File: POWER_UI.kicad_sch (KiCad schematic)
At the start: 46 parts

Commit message: fixed #1 , added protection circuit 5V selector jumper
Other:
- note added: "I2C I/O expander"
- note added: "Insulated high voltage input (max ??)"
- note added: "Insulated output"
- company: (none) -> Filippo Castellan, Alan Masutti
- title: (none) -> Think Embedded dev Board
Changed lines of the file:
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@@
 	(generator_version "9.0")
 	(paper "A4")
+	(title_block
+		(title "Think Embedded dev Board")
+		(date "2026-03-12")
+		(rev "1.0")
+		(company "Filippo Castellan, Alan Masutti")
+	)
 	(rectangle
 		(start 212.09 21.59)
@@
 		(stroke
 			(width 0)
-			(type default)
+			(type dash_dot)
 		)
 		(fill
@@
 		(stroke
 			(width 0)
-			(type default)
+			(type dash_dot)
 		)
 		(fill
@@
 		(stroke
 			(width 0)
-			(type default)
+			(type dash_dot)
 		)
 		(fill
@@
 		(stroke
 			(width 0)
-			(type default)
+			(type dash_dot)
 		)
 		(fill
@@
 		)
 	)
+	(text "Insulated output"
+		(exclude_from_sim no)
+		(at 219.964 20.066 0)
+		(effects
+			(font
+				(size 1.27 1.27)
+			)
+		)
+	)
+	(text "Insulated high voltage input (max ??)"
+		(exclude_from_sim no)
+		(at 132.842 20.066 0)
+		(effects
+			(font
+				(size 1.27 1.27)
+			)
+		)
+	)
+	(text "I2C I/O expander"
+		(exclude_from_sim no)
+		(at 33.782 20.32 0)
+		(effects
+			(font
+				(size 1.27 1.27)
+			)
+		)
+	)

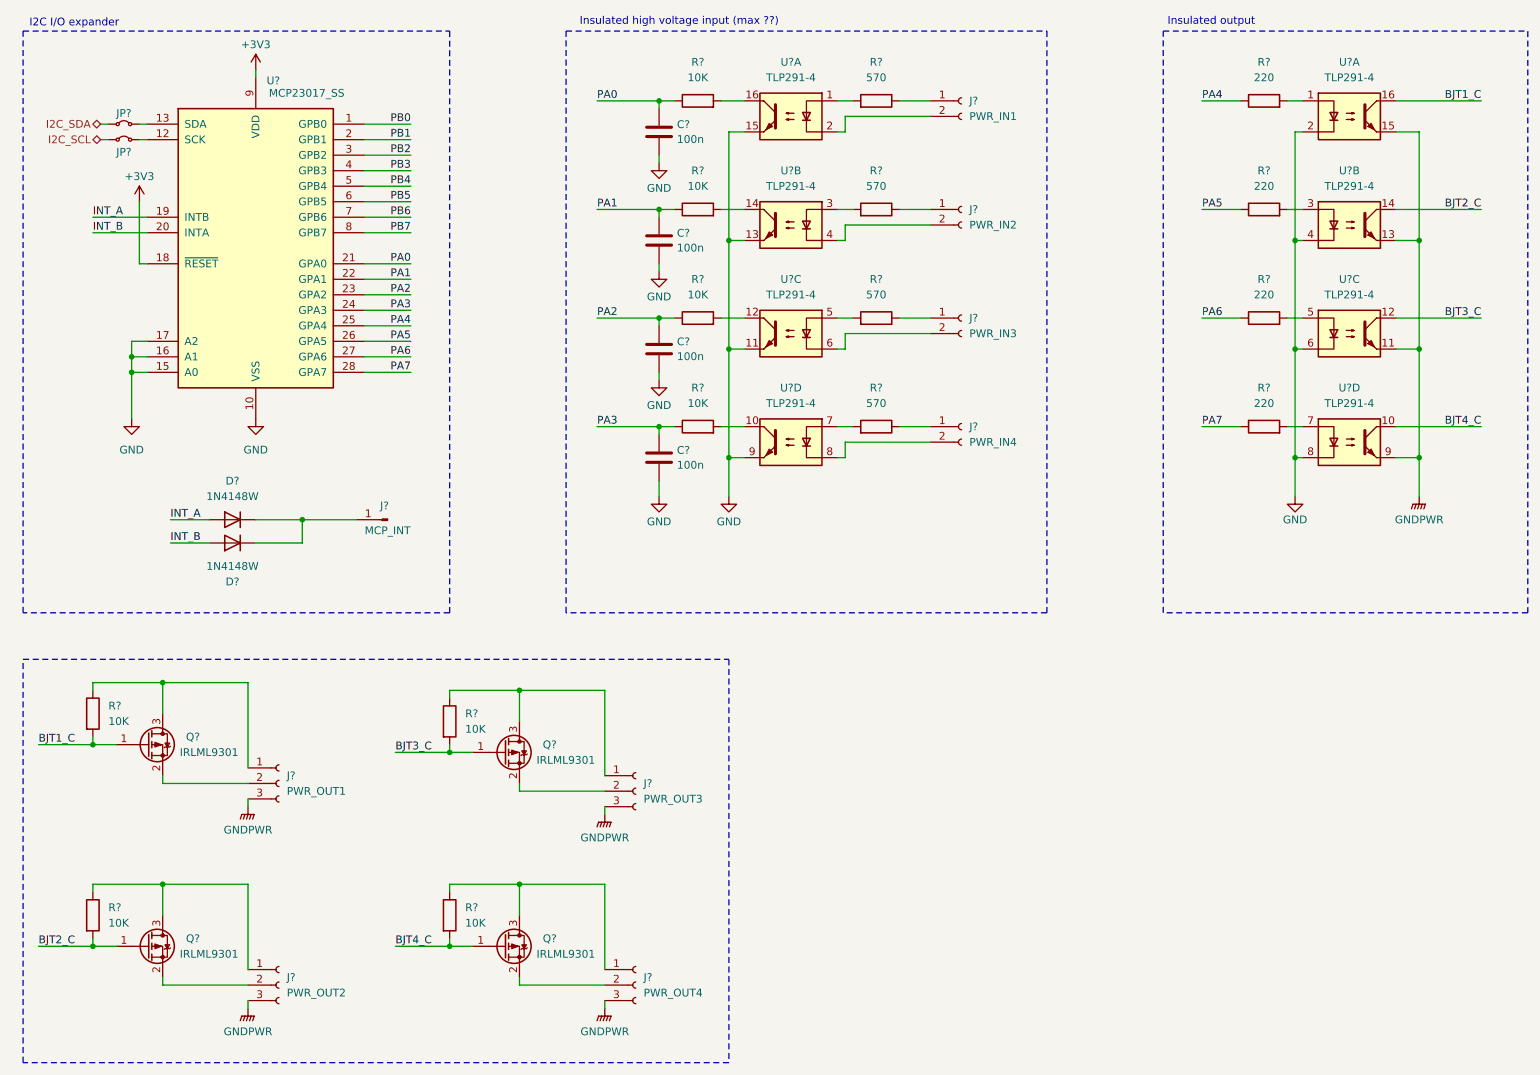
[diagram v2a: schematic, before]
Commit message: Changed the grounding of the opto-coupled power stage + Added UI connectors + Removed a Diode on the Power Sheet (Fixes #3)
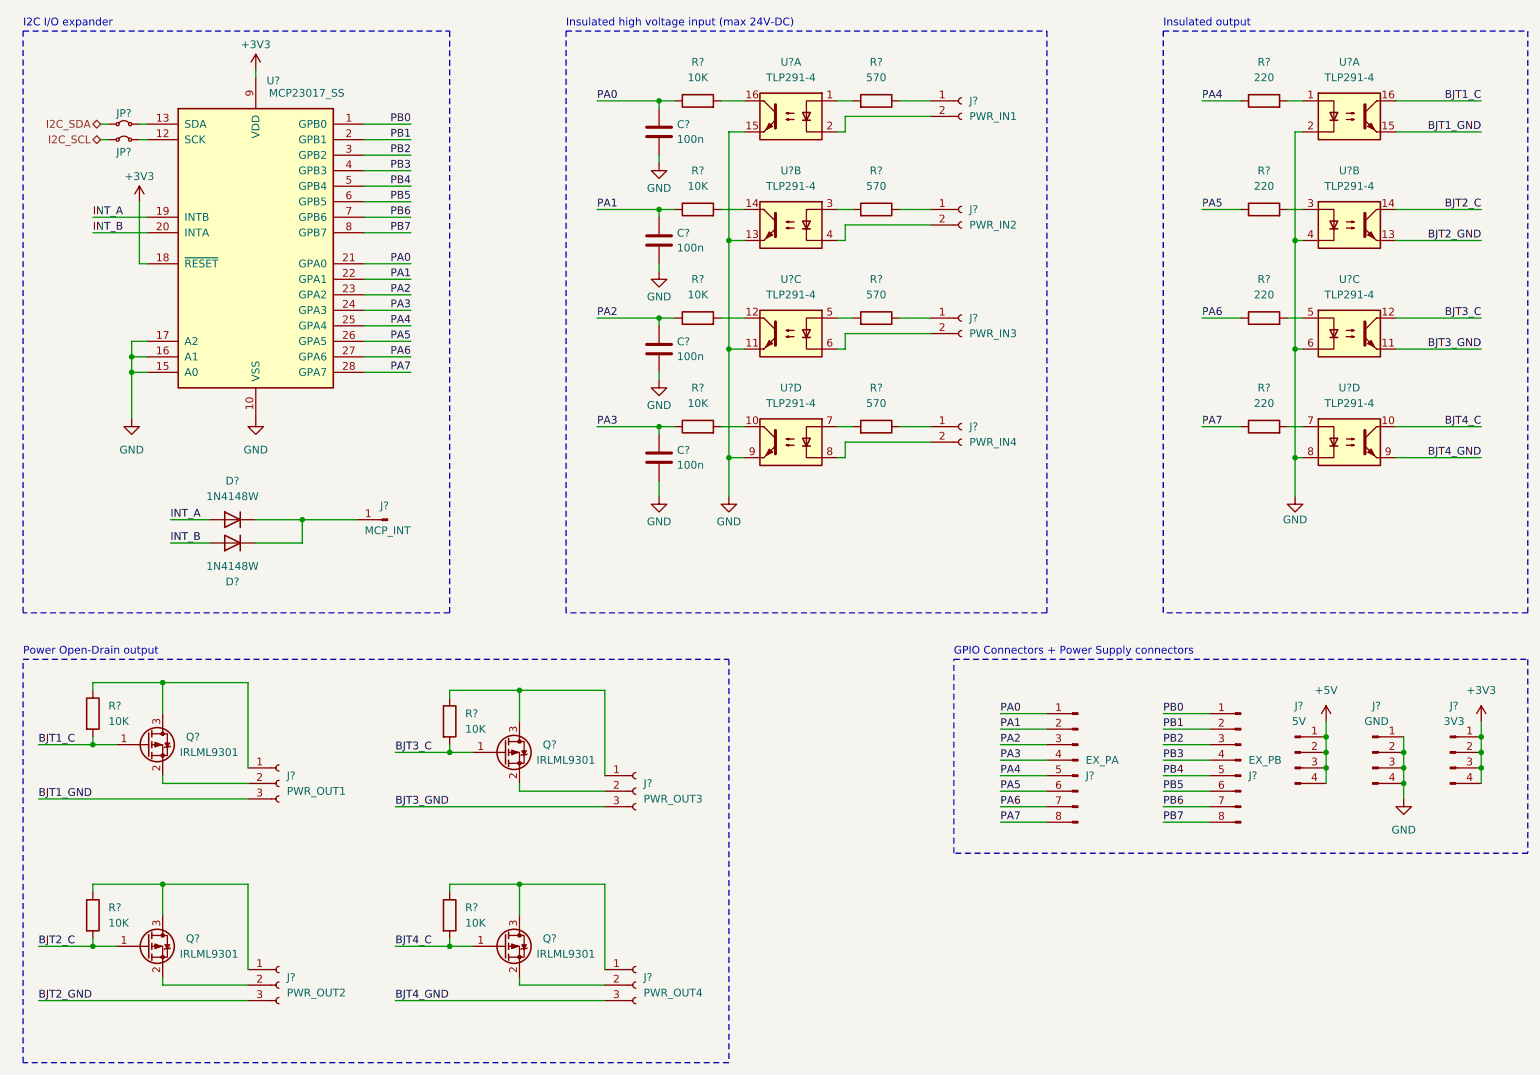
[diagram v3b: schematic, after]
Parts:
- added J?: GND, symbol Connector:Conn_01x04_Pin
- added J?: EX_PA, symbol Connector:Conn_01x08_Pin
- added J?: 3V3, symbol Connector:Conn_01x04_Pin
- added J?: EX_PB, symbol Connector:Conn_01x08_Pin
- added J?: 5V, symbol Connector:Conn_01x04_Pin
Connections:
- net +3V3: now also J?.1 (Pin_1), J?.2 (Pin_2), J?.3 (Pin_3), J?.4 (Pin_4)
- net GND: now also J?.1 (Pin_1), J?.2 (Pin_2), J?.3 (Pin_3), J?.4 (Pin_4)
- net PA0: now also J?.1 (Pin_1)
- net PA1: now also J?.2 (Pin_2)
- net PA2: now also J?.3 (Pin_3)
- net PA3: now also J?.4 (Pin_4)
- net PA4: now also J?.5 (Pin_5)
- net PA5: now also J?.6 (Pin_6)
- net PA6: now also J?.7 (Pin_7)
- net PA7: now also J?.8 (Pin_8)
- net PB0: now also J?.1 (Pin_1)
- net PB1: now also J?.2 (Pin_2)
- net PB2: now also J?.3 (Pin_3)
- net PB3: now also J?.4 (Pin_4)
- net PB4: now also J?.5 (Pin_5)
- net PB5: now also J?.6 (Pin_6)
- net PB6: now also J?.7 (Pin_7)
- net PB7: now also J?.8 (Pin_8)
- removed net GNDPWR: J?.3 (Pin_3), J?.3 (Pin_3), J?.3 (Pin_3), J?.3 (Pin_3), U?.11, U?.13, U?.15, U?.9
- new net +5V: J?.1 (Pin_1), J?.2 (Pin_2), J?.3 (Pin_3), J?.4 (Pin_4)
- new net BJT1_GND: J?.3 (Pin_3), U?.15
- new net BJT2_GND: J?.3 (Pin_3), U?.13
- new net BJT3_GND: J?.3 (Pin_3), U?.11
- new net BJT4_GND: J?.3 (Pin_3), U?.9
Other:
- note added: "GPIO Connectors + Power Supply connectors"
- note added: "Insulated high voltage input (max 24V-DC)"
- note added: "Power Open-Drain output"
- note removed: "Insulated high voltage input (max ??)"

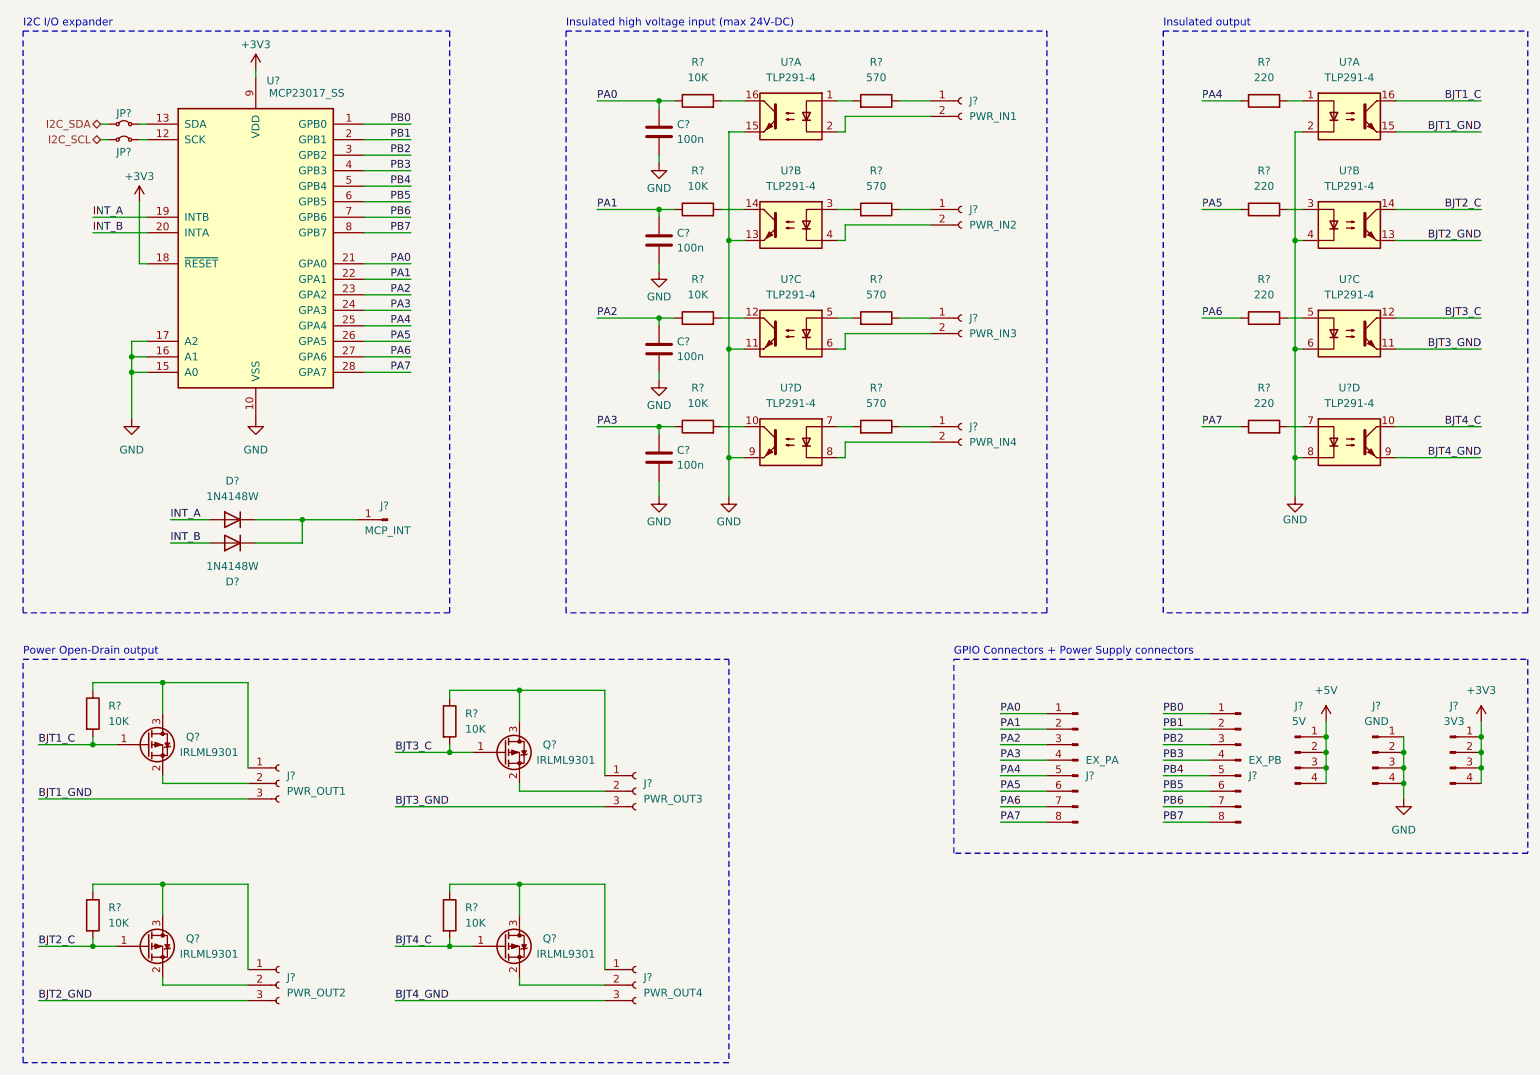
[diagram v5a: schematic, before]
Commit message: Fixed some schematic issues
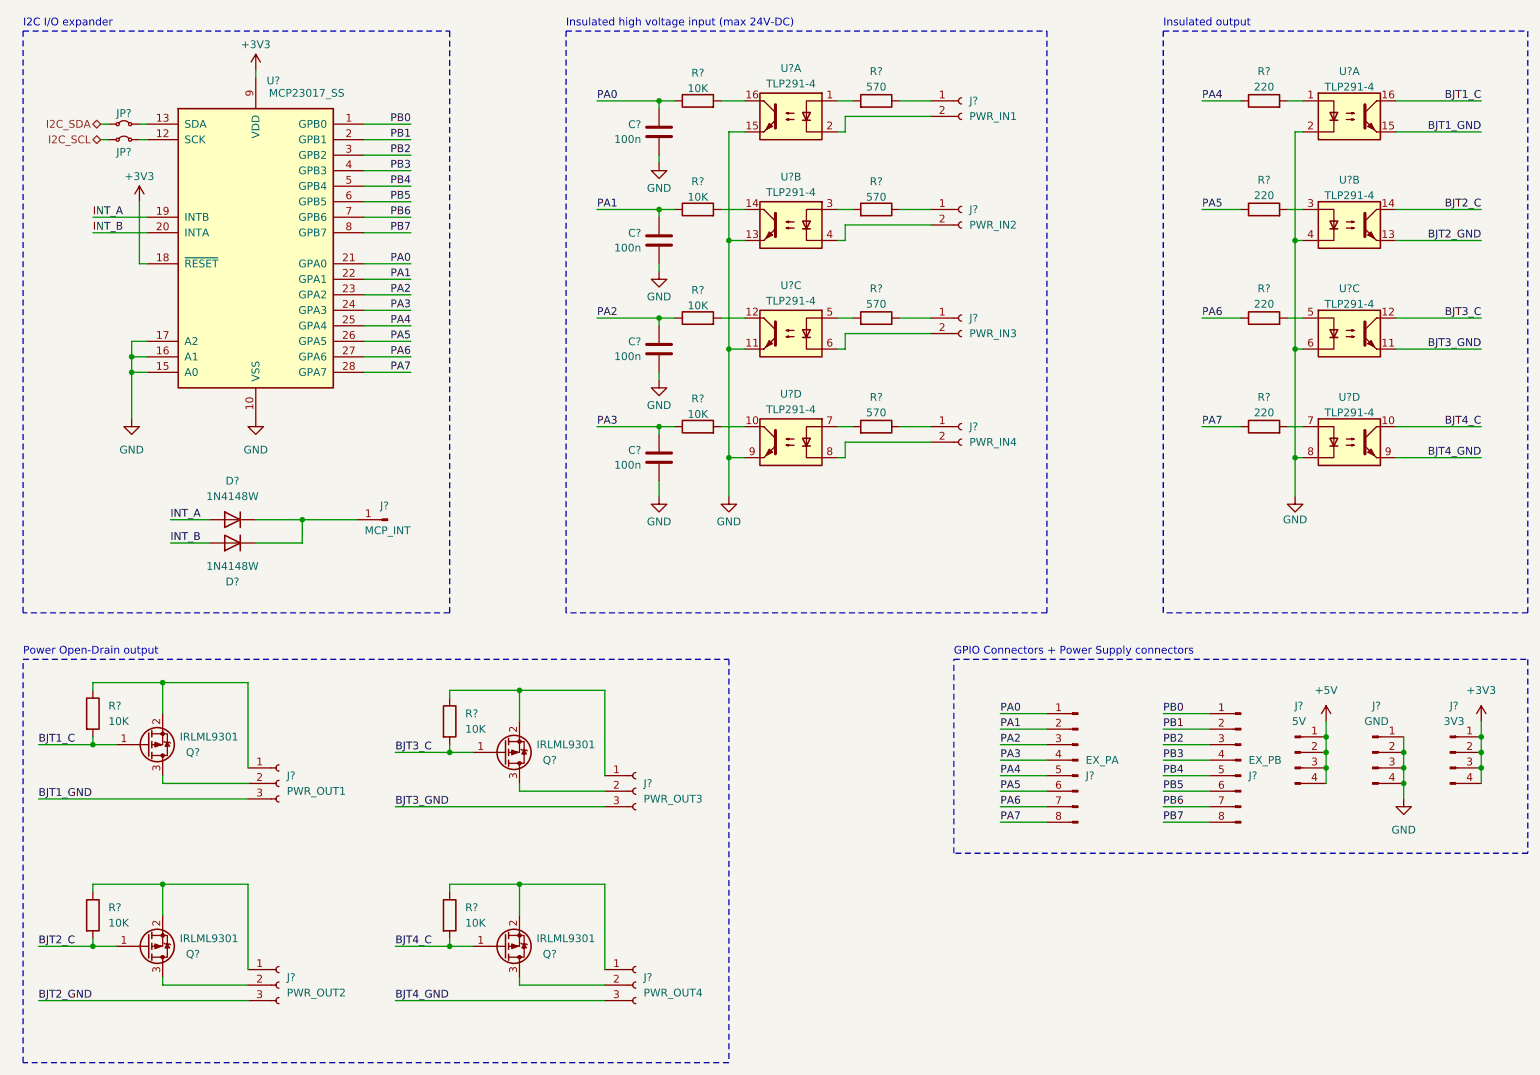
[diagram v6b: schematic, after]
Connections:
- net at J?.1 (Pin_1), R?.1: now also Q?.2 (S); no longer Q?.3 (D) (x2)
- net at J?.2 (Pin_2): now also Q?.3 (D); no longer Q?.2 (S) (x2)
- net at Q?.2 (S): now also J?.1 (Pin_1), R?.1; no longer J?.2 (Pin_2) (x2)
- new net: J?.2 (Pin_2), Q?.3 (D) (x2)

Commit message: Referenced the shematic and started the sourcing part
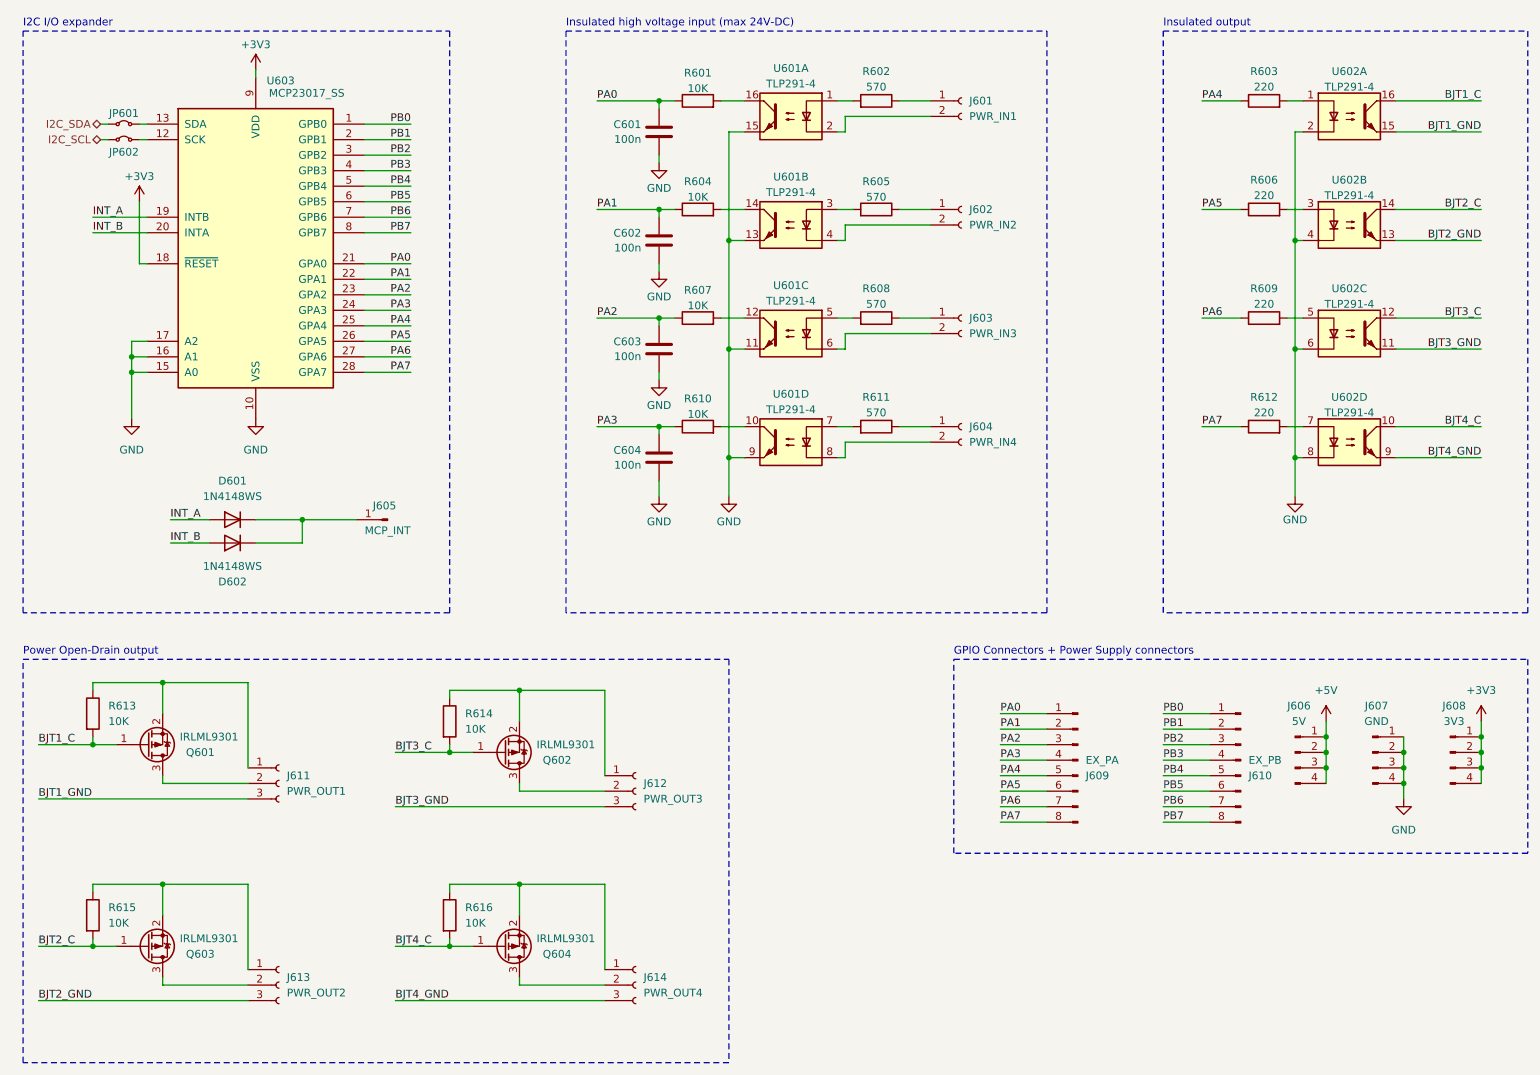
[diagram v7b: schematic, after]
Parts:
- C601, C602, C603, C604: renamed from C?; footprint Capacitor_SMD:C_0805_2012Metric_Pad1.18x1.45mm_HandSolder -> Capacitor_SMD:C_0603_1608Metric_Pad1.08x0.95mm_HandSolder; LCSC (none) -> C14663
- D601, D602: renamed from D?; value 1N4148W -> 1N4148WS; footprint Diode_SMD:D_SOD-123 -> Diode_SMD:D_SOD-323_HandSoldering; LCSC (none) -> C2128
- J601, J602, J603, J604: renamed from J?; footprint (none) -> Connector_PinHeader_2.54mm:PinHeader_1x02_P2.54mm_Vertical; LCSC (none) -> C492401
- J605: renamed from J?; footprint (none) -> Connector_PinHeader_2.54mm:PinHeader_1x01_P2.54mm_Vertical; LCSC (none) -> C492400
- J606, J607, J608: renamed from J?; footprint (none) -> Connector_PinHeader_2.54mm:PinHeader_1x04_P2.54mm_Vertical; LCSC (none) -> C492403
- J609, J610: renamed from J?; footprint (none) -> Connector_PinHeader_2.54mm:PinHeader_1x08_P2.54mm_Vertical; LCSC (none) -> C492407
- J611, J612, J613, J614: renamed from J?; footprint (none) -> Connector_PinHeader_2.54mm:PinHeader_1x03_P2.54mm_Vertical; LCSC (none) -> C492402
- R601, R604, R607, R610, R613, R614, R615, R616: renamed from R?; footprint (none) -> Resistor_SMD:R_0603_1608Metric_Pad0.98x0.95mm_HandSolder; LCSC (none) -> C25804
- R602, R605, R608, R611: renamed from R?; footprint (none) -> Resistor_SMD:R_0603_1608Metric_Pad0.98x0.95mm_HandSolder
- R603, R606, R609, R612: renamed from R?; footprint (none) -> Resistor_SMD:R_0603_1608Metric_Pad0.98x0.95mm_HandSolder; LCSC (none) -> C22962
- U601, U602: renamed from U?; LCSC (none) -> C60900
- U603: renamed from U?; LCSC (none) -> C506653
- gave numbers to parts that had none: 6
